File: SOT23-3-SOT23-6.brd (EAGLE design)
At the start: 20 x 10.2 mm, 8 parts

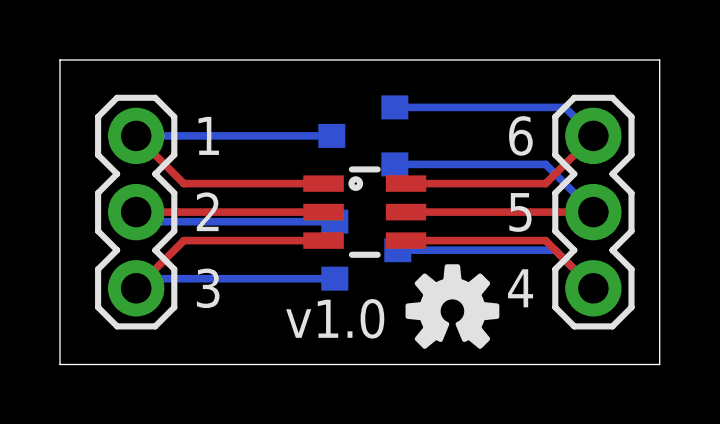
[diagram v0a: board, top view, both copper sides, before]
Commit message: Silk and board revision
Worked several silk screen issues and narrowed some boards.
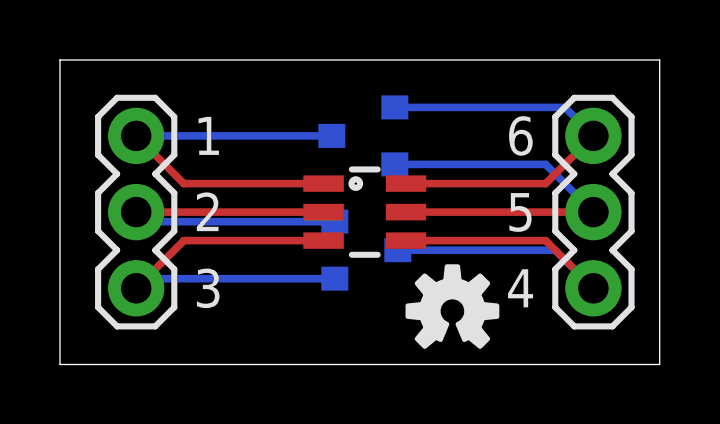
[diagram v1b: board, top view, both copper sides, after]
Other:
- board text removed: "v1.0"
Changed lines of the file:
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@@
 <text x="11.811" y="13.335" size="1.27" layer="22" rot="MR0">6</text>
 <text x="26.924" y="-3.048" size="1.778" layer="51">Kevin Neubauer</text>
-<text x="13.843" y="7.239" size="1.27" layer="21">v1.0</text>
 </plain>
 <attributes>
